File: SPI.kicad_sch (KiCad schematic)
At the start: 0 parts

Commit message: Update ldo.kicad_sch
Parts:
- added IC1: SRAM, SOIC127P600X175-8N, symbol group127:SRAM
- added J1: SD_Card, CUI_MSD-12-A, symbol group127:MSD-12-A
- added R1: 27, RESC2012X60N, symbol group127:Resistor
- added U1: EEPROM, SOIC8_ONS, symbol group127:CAT25160VI-GT3
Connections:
- new net: J1.CD, R1.2
- new net +3.3V: IC1.7 (~{HOLD_(SIO3)}), IC1.8 (VDD), J1.P4 (VDD), R1.1, U1.3 (*WP), U1.7 (*HOLD), U1.8 (VCC)
- new net CD/DAT3: J1.P2 (CD/DAT3)
- new net CMD: J1.P3 (CMD)
- new net CS EEPROM: U1.1 (*CS)
- new net DAT0: J1.P7 (DAT0)
- new net DAT1: J1.P8 (DAT1)
- new net DAT2: J1.P1 (DAT2)
- new net GND: IC1.4 (VSS), J1.G1 (COVER_GND), J1.G2 (COVER_GND__1), J1.G3 (COVER_GND__2), J1.G4 (COVER_GND__3), J1.G5 (COVER_GND__4), J1.G6 (COVER_GND__5), J1.P6 (VSS), U1.4 (VSS)
- new net MISO: IC1.2 (SO_(SIO1)), U1.2 (SO)
- new net MOSI: IC1.5 (SI(SIO0)), U1.5 (SI)
- new net SPI CLOCK: IC1.6 (SCK), J1.P5 (CLK), U1.6 (SCK)
- new net ~{CS} SRAM: IC1.1 (~{CS})
- no-connect marks 0 -> 1

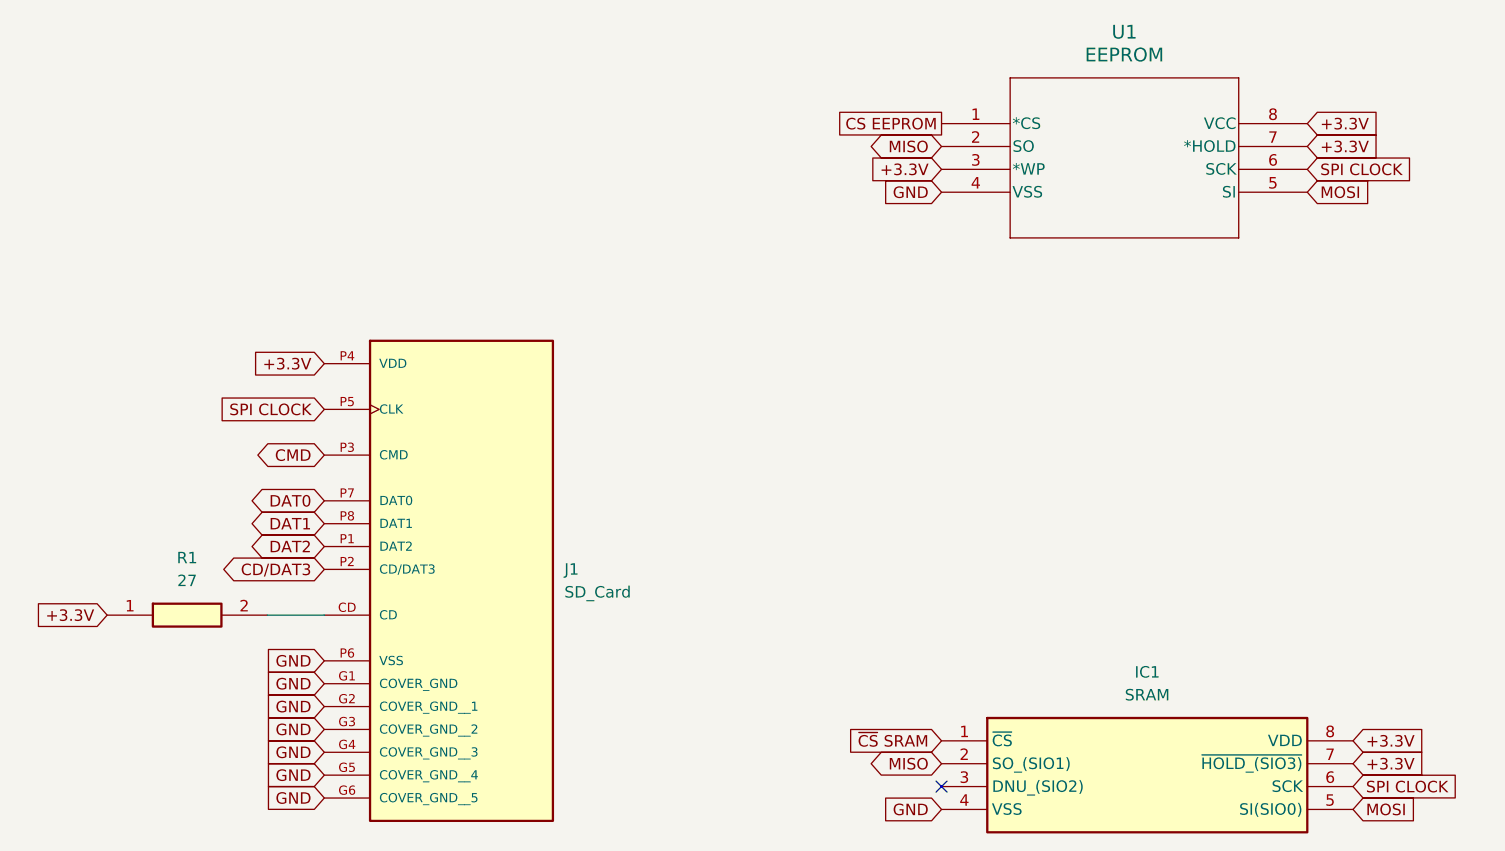
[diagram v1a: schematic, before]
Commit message: Put grounds on SPI
Changed ground net to symbols
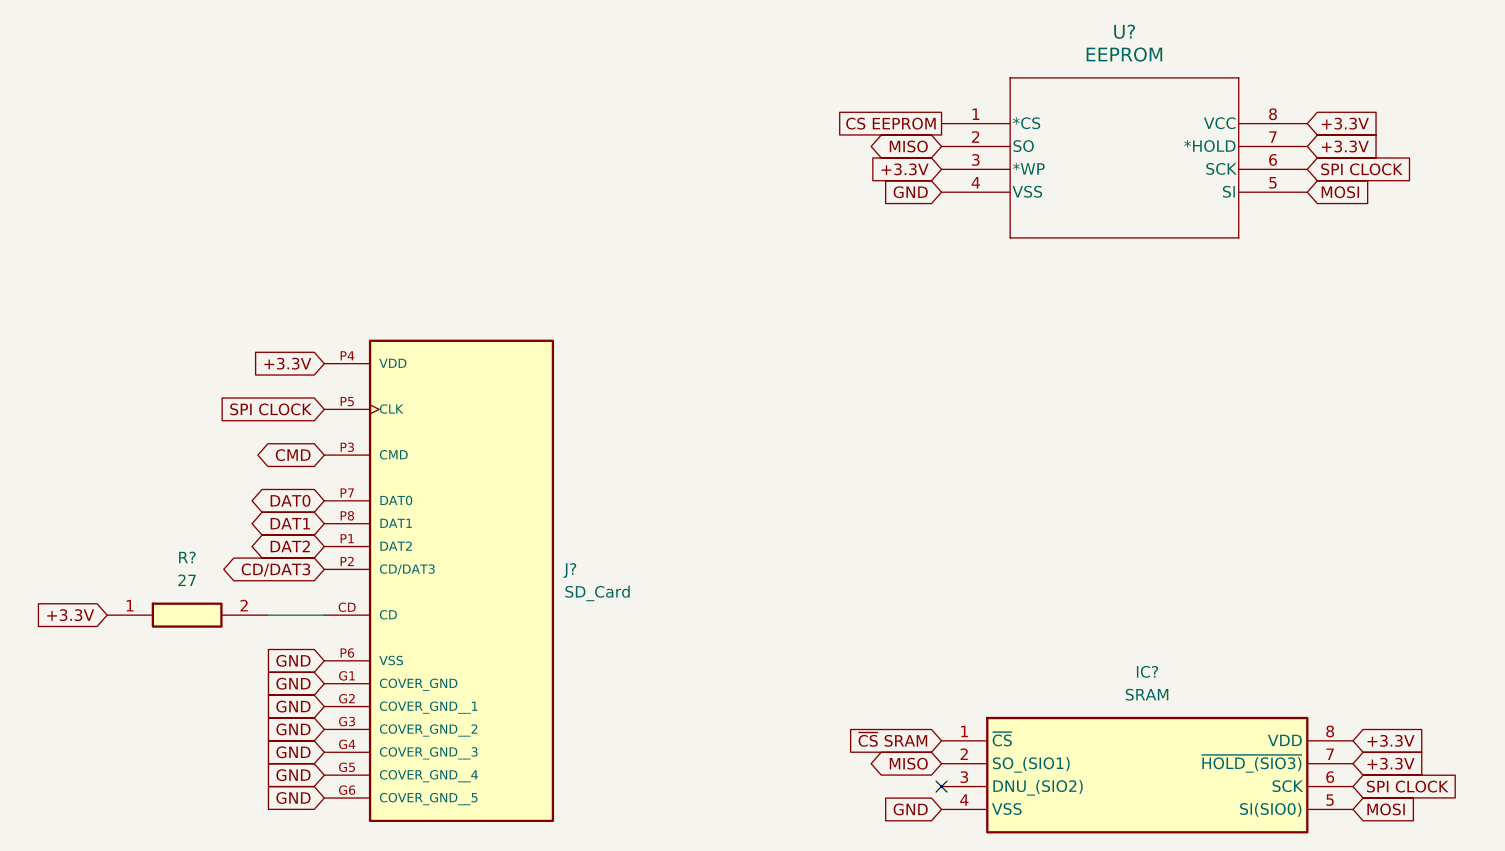
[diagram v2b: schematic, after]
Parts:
- renumbered IC1 to IC?, J1 to J?, R1 to R?, U1 to U?
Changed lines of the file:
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@@
 		(dnp no)
 		(fields_autoplaced yes)
-		(property "Reference" "IC1"
+		(property "Reference" "IC?"
 			(at 146.05 107.95 0)
 			(effects
@@
 		)
 		(instances
+			(project "harm_drone"
+				(path "/5ce3566e-4e0f-420e-9b0d-3952cd3c63fd/9ace3f70-8aef-468d-a7a3-d32e6ab166be"
+					(reference "IC?")
+					(unit 1)
+				)
+			)
 			(project ""
 				(path "/a1dacf80-5959-4abc-a7b3-75daab69d2bc"
@@
 		(dnp no)
 		(fields_autoplaced yes)
-		(property "Reference" "U1"
+		(property "Reference" "U?"
 			(at 143.51 36.83 0)
 			(effects
@@
 		)
 		(instances
+			(project "harm_drone"
+				(path "/5ce3566e-4e0f-420e-9b0d-3952cd3c63fd/9ace3f70-8aef-468d-a7a3-d32e6ab166be"
+					(reference "U?")
+					(unit 1)
+				)
+			)
 			(project ""
 				(path "/a1dacf80-5959-4abc-a7b3-75daab69d2bc"
@@
 		(dnp no)
 		(fields_autoplaced yes)
-		(property "Reference" "J1"
+		(property "Reference" "J?"
 			(at 81.28 96.5199 0)
 			(effects
@@
 		)
 		(instances
+			(project "harm_drone"
+				(path "/5ce3566e-4e0f-420e-9b0d-3952cd3c63fd/9ace3f70-8aef-468d-a7a3-d32e6ab166be"
+					(reference "J?")
+					(unit 1)
+				)
+			)
 			(project ""
 				(path "/a1dacf80-5959-4abc-a7b3-75daab69d2bc"
@@
 		(dnp no)
 		(fields_autoplaced yes)
-		(property "Reference" "R1"
+		(property "Reference" "R?"
 			(at 39.37 95.25 0)
 			(effects
@@
 		)
 		(instances
+			(project "harm_drone"
+				(path "/5ce3566e-4e0f-420e-9b0d-3952cd3c63fd/9ace3f70-8aef-468d-a7a3-d32e6ab166be"
+					(reference "R?")
+					(unit 1)
+				)
+			)
 			(project ""
 				(path "/a1dacf80-5959-4abc-a7b3-75daab69d2bc"
